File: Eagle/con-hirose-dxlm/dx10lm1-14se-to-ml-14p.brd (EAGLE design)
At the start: 31 x 36 mm, 2 parts, among them X1 HIROSE-DX10LM1-14SE

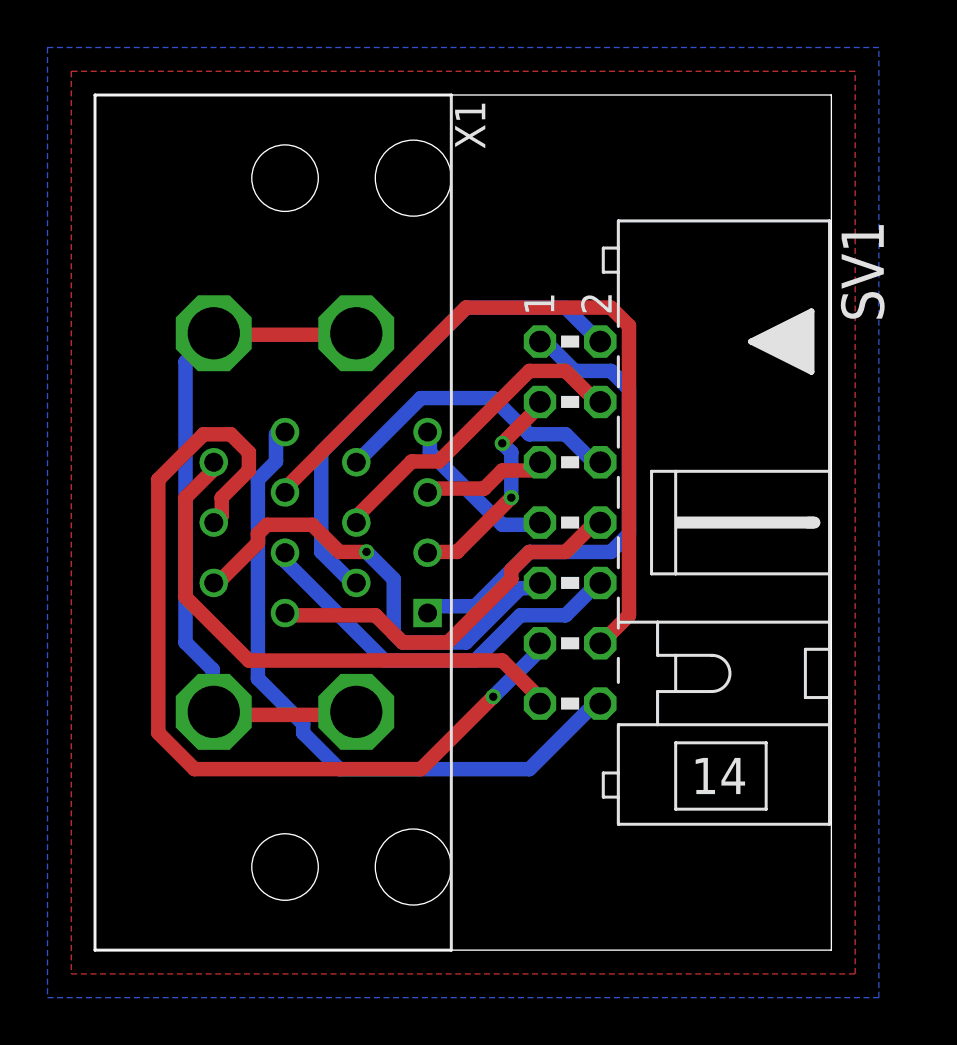
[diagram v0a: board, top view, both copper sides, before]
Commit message: Renewed D2ML adaptor.
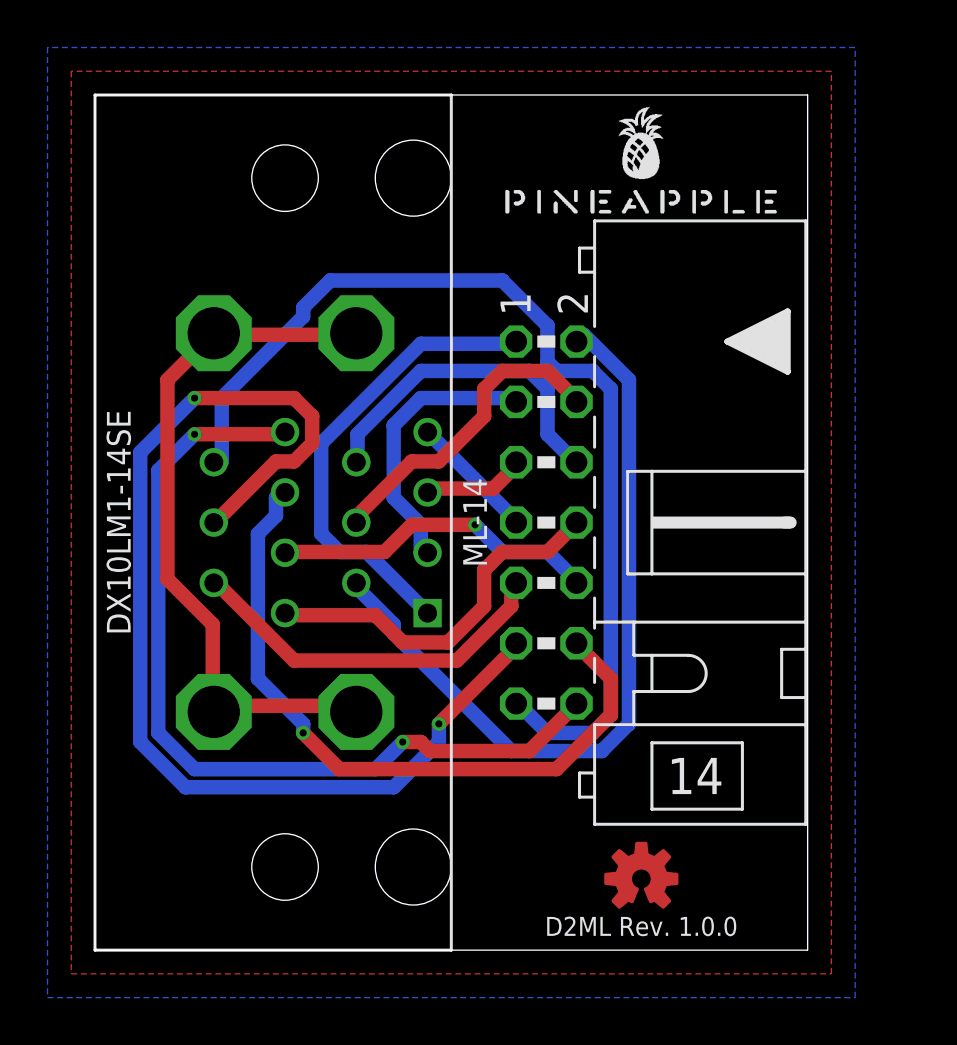
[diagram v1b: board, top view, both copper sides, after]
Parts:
- removed SV1: (no value), con-ml:ML14L
- added LOGO1: OSHW-LOGOS-COPPER, SparkFun-Aesthetics:OSHW-LOGO-S_COPPER
- added ML-14: (no value), con-ml:ML14L
- added U$1: PINEAPPLE450_SILK, pineapple:PINEAPPLE450_SILK
- renumbered X1 to DX10LM1-14SE
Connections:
- removed net N$1: DX10LM1-14SE.P$1, SV1.1
- removed net N$10: DX10LM1-14SE.P$6, SV1.6
- removed net N$11: DX10LM1-14SE.P$8, SV1.8
- removed net N$12: DX10LM1-14SE.P$10, SV1.10
- removed net N$13: DX10LM1-14SE.P$12, SV1.12
- removed net N$14: DX10LM1-14SE.P$14, SV1.14
- removed net N$2: DX10LM1-14SE.P$3, SV1.3
- removed net N$3: DX10LM1-14SE.P$5, SV1.5
- removed net N$4: DX10LM1-14SE.P$7, SV1.7
- removed net N$5: DX10LM1-14SE.P$9, SV1.9
- removed net N$6: DX10LM1-14SE.P$11, SV1.11
- removed net N$7: DX10LM1-14SE.P$13, SV1.13
- removed net N$8: DX10LM1-14SE.P$2, SV1.2
- removed net N$9: DX10LM1-14SE.P$4, SV1.4
- new net P1: DX10LM1-14SE.P$1, ML-14.1
- new net P10: DX10LM1-14SE.P$10, ML-14.10
- new net P11: DX10LM1-14SE.P$11, ML-14.11
- new net P12: DX10LM1-14SE.P$12, ML-14.12
- new net P13: DX10LM1-14SE.P$13, ML-14.13
- new net P14: DX10LM1-14SE.P$14, ML-14.14
- new net P2: DX10LM1-14SE.P$2, ML-14.2
- new net P3: DX10LM1-14SE.P$3, ML-14.3
- new net P4: DX10LM1-14SE.P$4, ML-14.4
- new net P5: DX10LM1-14SE.P$5, ML-14.5
- new net P6: DX10LM1-14SE.P$6, ML-14.6
- new net P7: DX10LM1-14SE.P$7, ML-14.7
- new net P8: DX10LM1-14SE.P$8, ML-14.8
- new net P9: DX10LM1-14SE.P$9, ML-14.9
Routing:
- net P11: track 0.00 -> 47.0 mm, vias 0 -> 2
- net P13: track 0.00 -> 43.0 mm
- net N$6: track 38.2 -> 0.00 mm, vias 1 -> 0
- net P14: track 0.00 -> 36.7 mm, vias 0 -> 2
- net P2: track 0.00 -> 32.8 mm
- net N$13: track 32.0 -> 0.00 mm
- net P12: track 0.00 -> 29.6 mm, vias 0 -> 1
- net N$14: track 28.3 -> 0.00 mm
- net N$7: track 23.0 -> 0.00 mm
- net N$8: track 21.0 -> 0.00 mm
- net N$1: track 20.6 -> 0.00 mm
- net P1: track 0.00 -> 19.6 mm
- net N$5: track 19.4 -> 0.00 mm, vias 1 -> 0
- net N$12: track 16.7 -> 0.00 mm
- net N$11: track 16.1 -> 0.00 mm
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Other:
- board size 31 x 36 mm -> 30 x 36 mm
- board text added: "D2ML Rev. 1.0.0"
